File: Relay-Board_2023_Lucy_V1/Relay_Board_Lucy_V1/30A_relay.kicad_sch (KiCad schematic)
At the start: 5 parts, among them K5 T9AV5L12-12, Q1 SI2302A-TPMSCT-ND

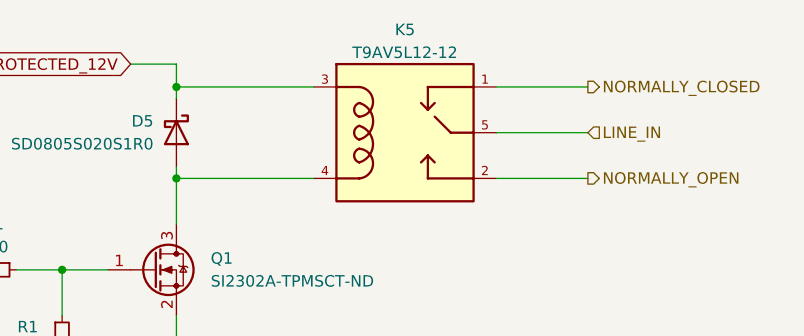
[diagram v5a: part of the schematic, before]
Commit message: Started work on the BOM file and I updated the lower current relays to work with 50A models
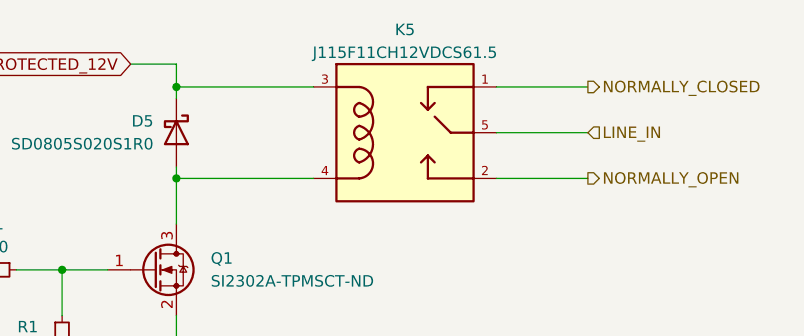
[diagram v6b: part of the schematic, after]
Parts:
- D5, Q1: Part# (none) -> digikey
- K5: value T9AV5L12-12 -> J115F11CH12VDCS61.5; footprint RB_FTP:T9AV5L12-12 -> RB_FTP:J115F11CH12VDCS61.5; Part# (none) -> digikey
- R1: Part# (none) -> C22962
- R1: Part# (none) -> C5250829
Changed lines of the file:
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@@
       (effects (font (size 1.27 1.27)) hide)
     )
-    (property "Datasheet" "~" (at 93.98 111.76 0)
+    (property "Datasheet" "https://datasheet.lcsc.com/lcsc/2206010130_UNI-ROYAL-Uniroyal-Elec-0603WAF2200T5E_C22962.pdf" (at 93.98 111.76 0)
       (effects (font (size 1.27 1.27)) hide)
     )
-    (property "Part#" "" (at 93.98 111.76 0)
+    (property "Part#" "C22962" (at 93.98 111.76 0)
       (effects (font (size 1.27 1.27)) hide)
     )
@@
       (effects (font (size 1.27 1.27)))
     )
-    (property "Value" "T9AV5L12-12" (at 139.7 87.63 0)
+    (property "Value" "J115F11CH12VDCS61.5" (at 139.7 87.63 0)
       (effects (font (size 1.27 1.27)))
     )
-    (property "Footprint" "RB_FTP:T9AV5L12-12" (at 139.7 96.52 0)
+    (property "Footprint" "RB_FTP:J115F11CH12VDCS61.5" (at 139.7 96.52 0)
       (effects (font (size 1.27 1.27)) (justify bottom) hide)
     )
     (property "Datasheet" "http://www.te.com/commerce/DocumentDelivery/DDEController?Action=showdoc&DocId=Data+Sheet%7F1308242_T9A%7F0915%7Fpdf%7FEnglish%7FENG_DS_1308242_T9A_0915.pdf%7F1423091-6" (at 139.7 109.22 0)
+      (effects (font (size 1.27 1.27)) hide)
+    )
+    (property "Part#" "digikey" (at 139.7 96.52 0)
       (effects (font (size 1.27 1.27)) hide)
     )
@@
       (effects (font (size 1.27 1.27)) hide)
     )
-    (property "Part#" "" (at 111.76 111.76 0)
+    (property "Part#" "digikey" (at 111.76 111.76 0)
       (effects (font (size 1.27 1.27)) hide)
     )
@@
       (effects (font (size 1.27 1.27)) hide)
     )
-    (property "Part#" "" (at 114.3 96.52 0)
+    (property "Part#" "digikey" (at 114.3 96.52 0)
       (effects (font (size 1.27 1.27)) hide)
     )
@@
       (effects (font (size 1.27 1.27)) hide)
     )
-    (property "Datasheet" "~" (at 101.6 119.38 0)
+    (property "Datasheet" "https://datasheet.lcsc.com/lcsc/2211251200_Ever-Ohms-Tech-TR0603D100KP0550Z_C5250829.pdf" (at 101.6 119.38 0)
       (effects (font (size 1.27 1.27)) hide)
     )
-    (property "Part#" "" (at 101.6 119.38 0)
+    (property "Part#" "C5250829" (at 101.6 119.38 0)
       (effects (font (size 1.27 1.27)) hide)
     )

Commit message: updated, created gerbers, created p&p, created BOM's
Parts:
- D5: Part# digikey -> 478-7800-1-ND
- K5: Part# digikey -> 2449-J115F11CH12VDCS61.5-ND
- Q1: Part# digikey -> SI2302A-TPMSCT-ND
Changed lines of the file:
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@@
       (effects (font (size 1.27 1.27)) hide)
     )
-    (property "Part#" "digikey" (at 139.7 96.52 0)
+    (property "Part#" "2449-J115F11CH12VDCS61.5-ND" (at 139.7 96.52 0)
       (effects (font (size 1.27 1.27)) hide)
     )
@@
       (effects (font (size 1.27 1.27)) hide)
     )
-    (property "Part#" "digikey" (at 111.76 111.76 0)
+    (property "Part#" "SI2302A-TPMSCT-ND" (at 111.76 111.76 0)
       (effects (font (size 1.27 1.27)) hide)
     )
@@
       (effects (font (size 1.27 1.27)) hide)
     )
-    (property "Part#" "digikey" (at 114.3 96.52 0)
+    (property "Part#" "478-7800-1-ND" (at 114.3 96.52 0)
       (effects (font (size 1.27 1.27)) hide)
     )

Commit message: update
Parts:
- added C9: 100n, Capacitor_SMD:C_0603_1608Metric, symbol Device:C_Small
- added R1: 470, Resistor_SMD:R_0603_1608Metric, symbol Device:R_Small
- added U8: H11L1SR2M, RB_FTP:IC_H11L1SR2M, symbol RB_PARTS:H11L1SR2M
- R1: value 220 -> 10k
- R1: value 100k -> 10k
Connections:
- net GNDA: now also C9.2, U8.2, U8.5
- net UNPROTECTED_12V: now also C9.1, U8.6
- net RLY_ENBL: no longer names the net of R1.2
- net RLY_ENBL: now also U8.4
- new net: R1.1, U8.1
- new net ~{RLY_ENBL}: R1.2
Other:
- moved on the sheet: D5, K5, Q1, R1
